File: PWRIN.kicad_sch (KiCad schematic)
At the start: 16 parts, among them J1 SM02B-SRSS-TB(LF)(SN), U13 TPS63020DSJR, U5 AP2112K-3.3

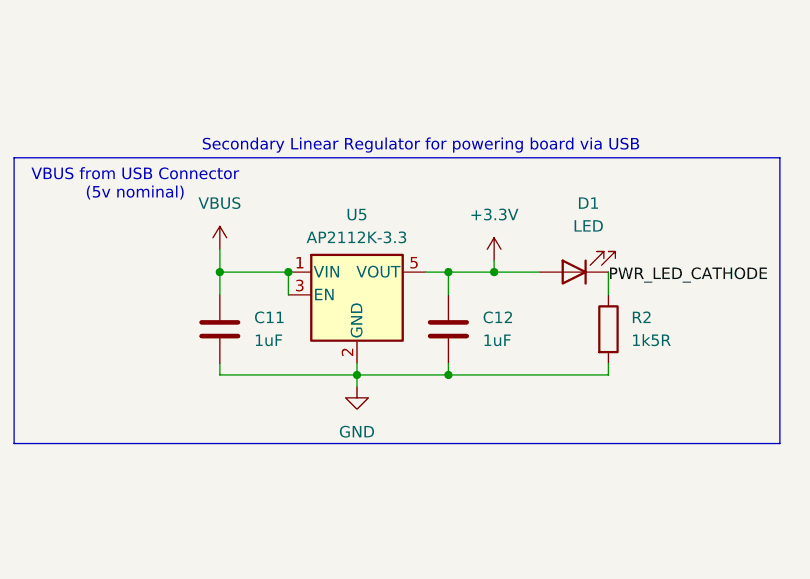
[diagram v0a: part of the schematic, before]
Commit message: feat(pcb) cleanup and improve reliability
add pullups to SPI CS lines, rearrange board slightly, add V1.0 silkscreen, increase size of VBUS input cap
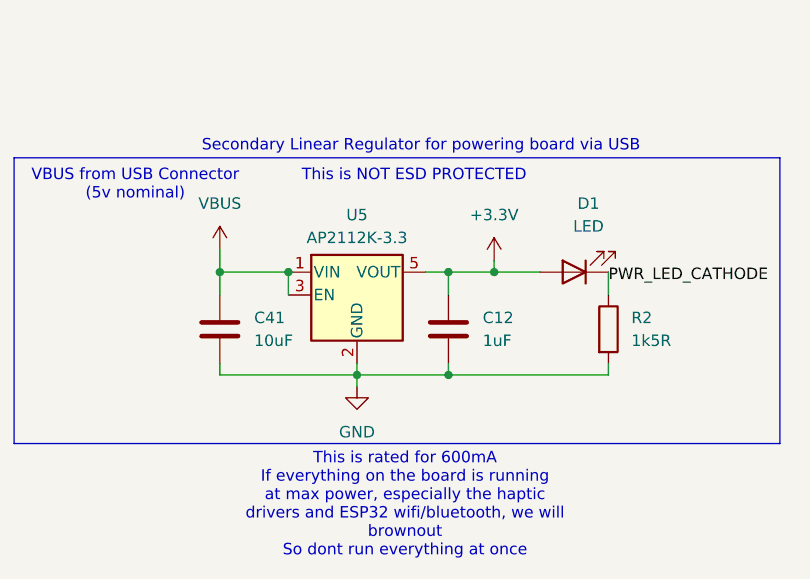
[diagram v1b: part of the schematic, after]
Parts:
- removed C11: 1uF, Capacitor_SMD:C_0402_1005Metric, symbol Device:C
- added C41: 10uF, Capacitor_SMD:C_0603_1608Metric, symbol Device:C
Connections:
- net GND: now also C41.2
- net VBUS: now also C41.1
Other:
- note added: "This is NOT ESD PROTECTED"
- note added: "This is rated for 600mA If everything on the board is running at max power, especially the haptic drivers and ESP32 wifi/bluetooth, we will brownout So dont run everything at once"
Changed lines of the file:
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@@
+		)
+	)
+	(text "This is NOT ESD PROTECTED"
+		(exclude_from_sim no)
+		(at 73.66 130.302 0)
+		(effects
+			(font
+				(size 1.27 1.27)
+			)
 		)
 	)
@@
 		(exclude_from_sim no)
 		(at 202.946 90.424 0)
+		(effects
+			(font
+				(size 1.27 1.27)
+			)
+		)
+	)
+	(text "This is rated for 600mA\nIf everything on the board is running\nat max power, especially the haptic\ndrivers and ESP32 wifi/bluetooth, we will\nbrownout\nSo dont run everything at once"
+		(exclude_from_sim no)
+		(at 72.644 166.878 0)
 		(effects
 			(font
@@
 				(path "/bcb46d91-82bf-45dd-a940-c6de67888d6a/4872fb63-baee-41a4-9464-e6cc8d4aec48"
 					(reference "R12")
-					(unit 1)
-				)
-			)
-		)
-	)
-	(symbol
-		(lib_id "Device:C")
-		(at 52.07 147.32 0)
-		(unit 1)
-		(exclude_from_sim no)
-		(in_bom yes)
-		(on_board yes)
-		(dnp no)
-		(fields_autoplaced yes)
-		(property "Reference" "C11"
-			(at 55.88 146.0499 0)
-			(effects
-				(font
-					(size 1.27 1.27)
-				)
-				(justify left)
-			)
-		)
-		(property "Value" "1uF"
-			(at 55.88 148.5899 0)
-			(effects
-				(font
-					(size 1.27 1.27)
-				)
-				(justify left)
-			)
-		)
-		(property "Footprint" "Capacitor_SMD:C_0402_1005Metric"
-			(at 53.0352 151.13 0)
-			(effects
-				(font
-					(size 1.27 1.27)
-				)
-				(hide yes)
-			)
-		)
-		(property "Datasheet" "~"
-			(at 52.07 147.32 0)
-			(effects
-				(font
-					(size 1.27 1.27)
-				)
-				(hide yes)
-			)
-		)
-		(property "Description" "Unpolarized capacitor"
-			(at 52.07 147.32 0)
-			(effects
-				(font
-					(size 1.27 1.27)
-				)
-				(hide yes)
-			)
-		)
-		(pin "1"
-		)
-		(pin "2"
-		)
-		(instances
-			(project "Marcus's ESP32 Dev Board"
-				(path "/bcb46d91-82bf-45dd-a940-c6de67888d6a/4872fb63-baee-41a4-9464-e6cc8d4aec48"
-					(reference "C11")
 					(unit 1)
 				)
@@
 					(unit 1)
 				)
+			)
+		)
+	)
+	(symbol
+		(lib_id "Device:C")
+		(at 52.07 147.32 0)
+		(unit 1)
+		(exclude_from_sim no)
+		(in_bom yes)
+		(on_board yes)
+		(dnp no)
+		(fields_autoplaced yes)
+		(property "Reference" "C41"
+			(at 55.88 146.0499 0)
+			(effects
+				(font
+					(size 1.27 1.27)
+				)
+				(justify left)
+			)
+		)
+		(property "Value" "10uF"
+			(at 55.88 148.5899 0)
+			(effects
+				(font
+					(size 1.27 1.27)
+				)
+				(justify left)
+			)
+		)
+		(property "Footprint" "Capacitor_SMD:C_0603_1608Metric"
+			(at 53.0352 151.13 0)
+			(effects
+				(font
+					(size 1.27 1.27)
+				)
+				(hide yes)
+			)
+		)
+		(property "Datasheet" "~"
+			(at 52.07 147.32 0)
+			(effects
+				(font
+					(size 1.27 1.27)
+				)
+				(hide yes)
+			)
+		)
+		(property "Description" "Unpolarized capacitor"
+			(at 52.07 147.32 0)
+			(effects
+				(font
+					(size 1.27 1.27)
+				)
+				(hide yes)
+			)
+		)
+		(pin "2"
+		)
+		(pin "1"
+		)
+		(instances
+			(project "Marcus's ESP32 Dev Board"
+				(path "/bcb46d91-82bf-45dd-a940-c6de67888d6a/4872fb63-baee-41a4-9464-e6cc8d4aec48"
+					(reference "C41")
+					(unit 1)
+				)
